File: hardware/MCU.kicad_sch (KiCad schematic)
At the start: 5 parts

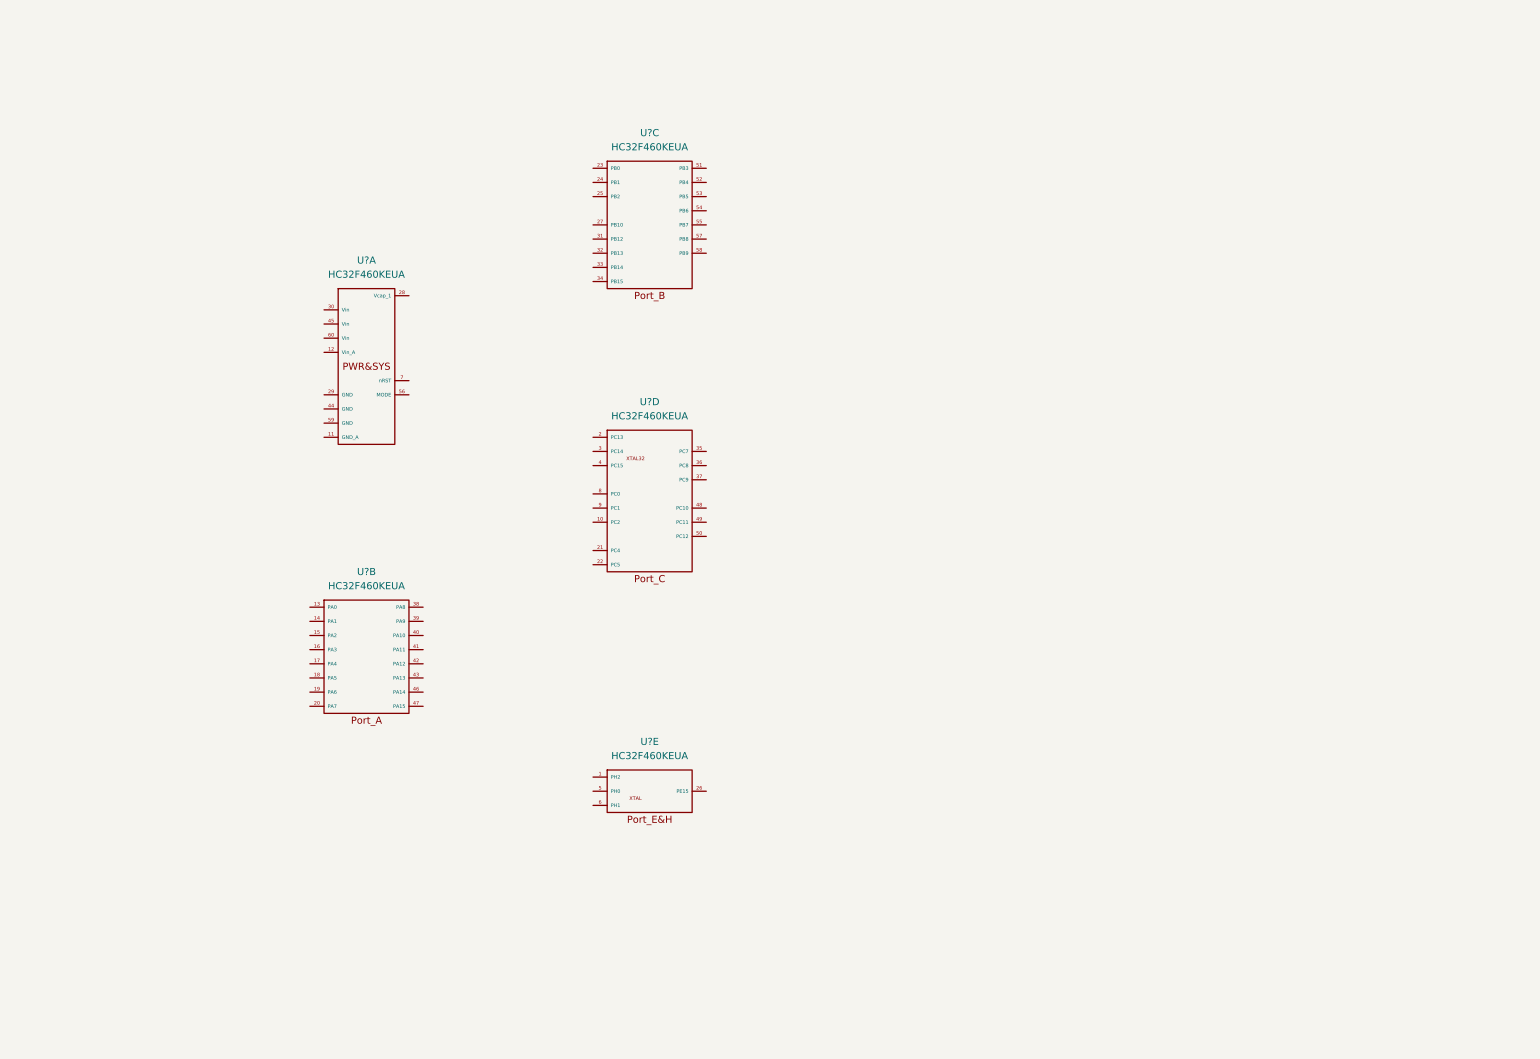
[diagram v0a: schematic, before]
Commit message: Update MCU and Base_PWR.
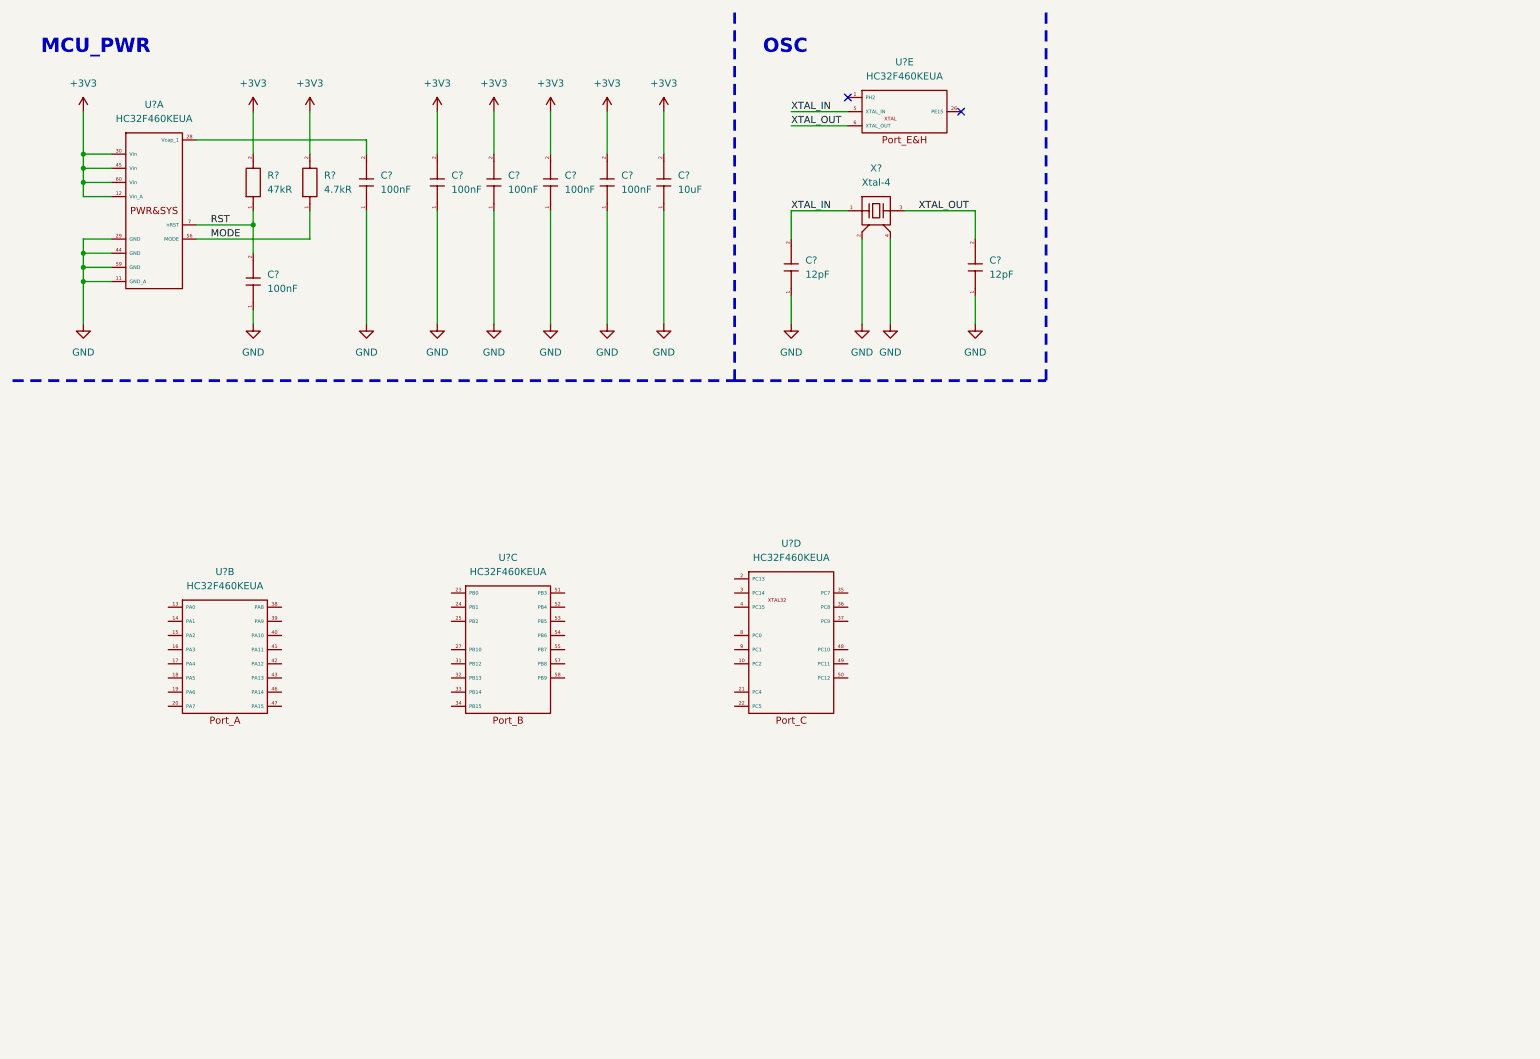
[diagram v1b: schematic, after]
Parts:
- added C? (x6): 100nF, GENERAL_RCL_SMD:C0402(1005M), symbol Basic_passive_components:Capacitor
- added C?: 10uF, GENERAL_RCL_SMD:C0603(1608M), symbol Basic_passive_components:Capacitor
- added C? (x2): 12pF, GENERAL_RCL_SMD:C0402(1005M), symbol Basic_passive_components:Capacitor
- added R?: 4.7kR, GENERAL_RCL_SMD:C0402(1005M), symbol Basic_passive_components:Resistor
- added R?: 47kR, GENERAL_RCL_SMD:C0402(1005M), symbol Basic_passive_components:Resistor
- added X?: Xtal-4, symbol Basic_crystal_and_oscillator:Xtal-4
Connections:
- net XTAL_IN: now reaches U?.5 (PH0)
- net XTAL_IN: now also C?.2, X?.1
- net XTAL_OUT: now reaches U?.6 (PH1)
- net XTAL_OUT: now also C?.2, X?.3
- net GND: now reaches U?.11 (GND_A)
- net GND: now also U?.29 (GND), U?.44 (GND), U?.59 (GND), C?.1, C?.1, C?.1, C?.1, C?.1, C?.1, C?.1, C?.1, C?.1, X?.2, X?.4
- net +3V3: now reaches U?.12 (Vin_A)
- net +3V3: now also U?.30 (Vin), U?.45 (Vin), U?.60 (Vin), C?.2, C?.2, C?.2, C?.2, C?.2, R?.2, R?.2
- net at U?.28 (Vcap_1): now also C?.2
- net MODE: now reaches U?.56 (MODE)
- net MODE: now also R?.1
- net RST: now reaches U?.7 (nRST)
- net RST: now also C?.2, R?.1
- no-connect marks 0 -> 2
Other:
- note added: "MCU_PWR"
- note added: "OSC"
- moved on the sheet: U?A, U?B, U?C, U?D, U?E

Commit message: Daily update
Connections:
- net GND: now also U?.EP
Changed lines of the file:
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@@
   (junction (at 25.4 60.96) (diameter 0) (color 0 0 0 0)
+  )
+  (junction (at 25.4 53.34) (diameter 0) (color 0 0 0 0)
   )
   (junction (at 55.88 50.8) (diameter 0) (color 0 0 0 0)
@@
     (stroke (width 0) (type default) (color 0 0 0 0))
   )
+  (wire (pts (xy 30.48 50.8) (xy 25.4 50.8))
+    (stroke (width 0) (type default) (color 0 0 0 0))
+  )
   (wire (pts (xy 25.4 43.18) (xy 25.4 45.72))
+    (stroke (width 0) (type default) (color 0 0 0 0))
+  )
+  (wire (pts (xy 25.4 50.8) (xy 25.4 53.34))
     (stroke (width 0) (type default) (color 0 0 0 0))
   )
@@
     (pin "4")
   )
-  (symbol (lib_id "Integrated-circuit_micro-controller:HC32F460KEUA") (at 38.1 48.26 0) (unit 1)
+  (symbol (lib_name "HC32F460KEUA_1") (lib_id "Integrated-circuit_micro-controller:HC32F460KEUA") (at 38.1 48.26 0) (unit 1)
     (in_bom yes) (on_board yes) (fields_autoplaced)
     (property "Reference" "U?" (id 0) (at 38.1 29.21 0))
@@
     (pin "60")
     (pin "7")
+    (pin "EP")
     (pin "13")
     (pin "14")

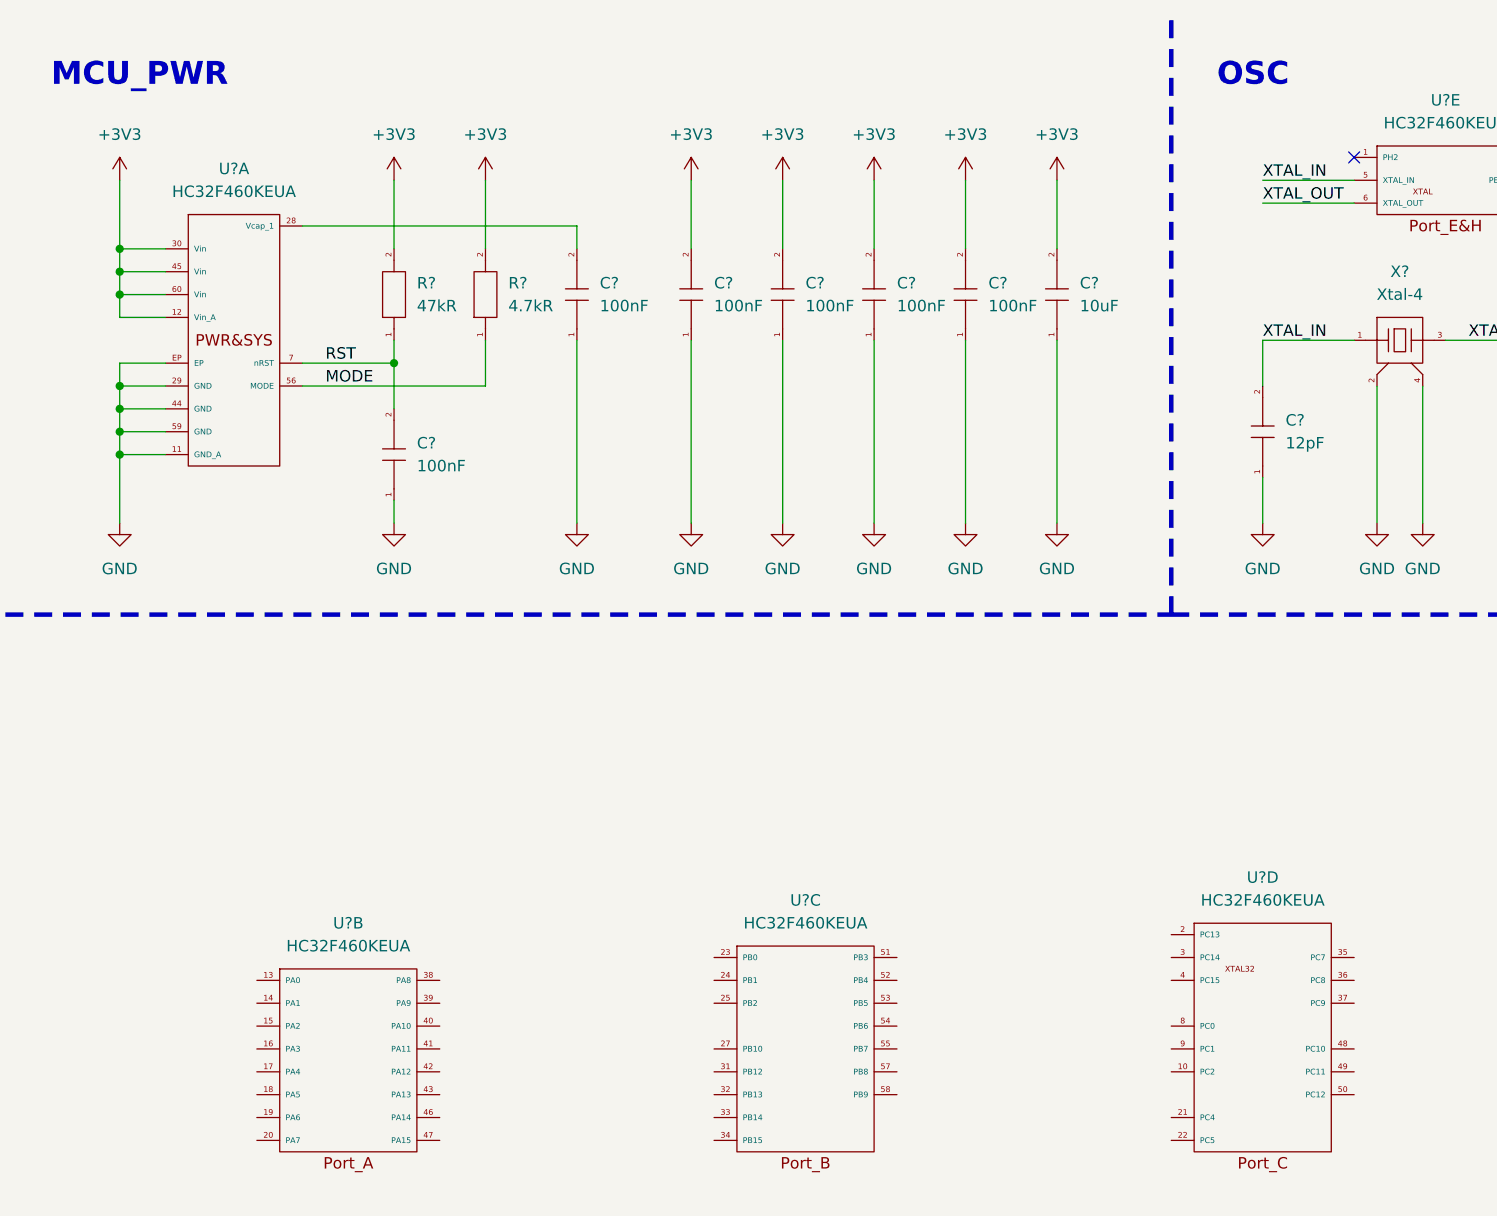
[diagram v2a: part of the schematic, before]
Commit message: Update symbols
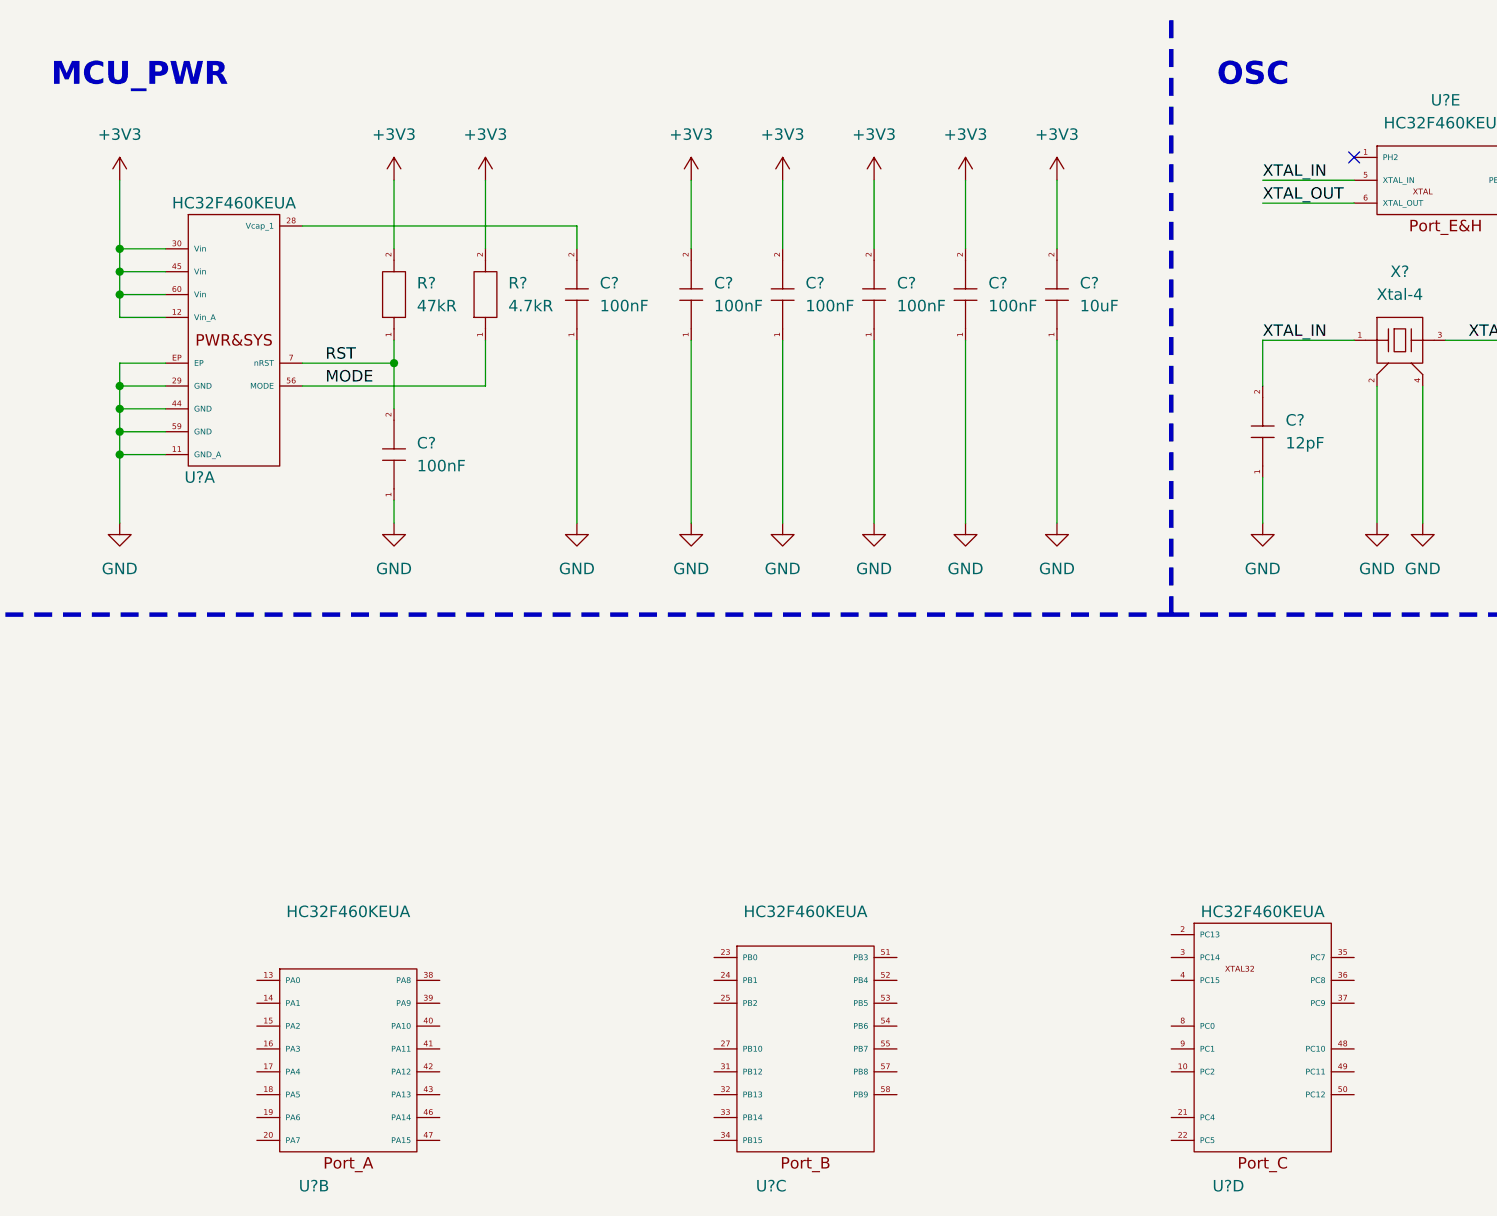
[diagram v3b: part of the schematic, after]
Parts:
- U? (x5): footprint GENERAL_MIDDLE-SEMI_SMD:QFN-7070_60 -> 004_GN_MIDDLE-SEMI_SMD:QFN-60_7070; symbol Integrated-circuit_micro-controller:HC32F460KEUA -> 107_IntegratedCircuit_MicroController:HC32F460KEUA; Symbol type (none) -> Specified Device

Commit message: Nightly update
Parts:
- removed C? (x4): 100nF, GENERAL_RCL_SMD:C0402(1005M), symbol Basic_passive_components:Capacitor
- removed C?: 10uF, GENERAL_RCL_SMD:C0603(1608M), symbol Basic_passive_components:Capacitor
- removed C?: 12pF, GENERAL_RCL_SMD:C0402(1005M), symbol Basic_passive_components:Capacitor
- added C? (x5): 100nF, 001_GN_RCL_SMD:C0402(1005M), symbol 001_Basic_PassiveComponents:101_Capacitor
- added C?: 12pF, 001_GN_RCL_SMD:C0402(1005M), symbol 001_Basic_PassiveComponents:101_Capacitor
- C? (x3): footprint GENERAL_RCL_SMD:C0402(1005M) -> 001_GN_RCL_SMD:C0402(1005M); symbol Basic_passive_components:Capacitor -> 001_Basic_PassiveComponents:101_Capacitor; Symbol type (none) -> Alternate Source
- R? (x2): footprint GENERAL_RCL_SMD:C0402(1005M) -> 001_GN_RCL_SMD:R0402(1005M); symbol Basic_passive_components:Resistor -> 001_Basic_PassiveComponents:001_Resistor; Symbol type (none) -> Alternate Source
- X?: footprint (none) -> 006_GN_XTAL_OSC_SMD:SMD-4_3225; symbol Basic_crystal_and_oscillator:Xtal-4 -> 003_Basic_CrystalAndOscillator:002_Xtal-4; Symbol type (none) -> Alternate Source
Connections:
- net +3V3: now also C?.2, C?.2, C?.2, C?.2, C?.2
- net GND: now also C?.1, C?.1, C?.1, C?.1, C?.1, C?.1
- net XTAL_OUT: now also C?.2

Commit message: Nightly Update
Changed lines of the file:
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@@
   (symbol (lib_id "107_IntegratedCircuit_MicroController:HC32F460KEUA") (at 152.4 127 0) (unit 4)
     (in_bom yes) (on_board yes) (fields_autoplaced)
-    (property "Reference" "U?" (id 0) (at 148.59 142.24 0))
-    (property "Value" "HC32F460KEUA" (id 1) (at 152.4 111.76 0))
+    (property "Reference" "U?" (id 0) (at 152.4 107.95 0))
+    (property "Value" "HC32F460KEUA" (id 1) (at 152.4 110.49 0))
     (property "Footprint" "004_GN_MIDDLE-SEMI_SMD:QFN-60_7070" (id 2) (at 152.4 109.22 0)
       (effects (font (size 1.27 1.27)) hide)
@@
   (symbol (lib_id "107_IntegratedCircuit_MicroController:HC32F460KEUA") (at 101.6 127 0) (unit 3)
     (in_bom yes) (on_board yes) (fields_autoplaced)
-    (property "Reference" "U?" (id 0) (at 97.79 142.24 0))
-    (property "Value" "HC32F460KEUA" (id 1) (at 101.6 111.76 0))
+    (property "Reference" "U?" (id 0) (at 101.6 110.49 0))
+    (property "Value" "HC32F460KEUA" (id 1) (at 101.6 113.03 0))
     (property "Footprint" "004_GN_MIDDLE-SEMI_SMD:QFN-60_7070" (id 2) (at 101.6 109.22 0)
       (effects (font (size 1.27 1.27)) hide)
@@
   (symbol (lib_id "107_IntegratedCircuit_MicroController:HC32F460KEUA") (at 38.1 48.26 0) (unit 1)
     (in_bom yes) (on_board yes) (fields_autoplaced)
-    (property "Reference" "U?" (id 0) (at 34.29 63.5 0))
-    (property "Value" "HC32F460KEUA" (id 1) (at 38.1 33.02 0))
+    (property "Reference" "U?" (id 0) (at 38.1 29.21 0))
+    (property "Value" "HC32F460KEUA" (id 1) (at 38.1 31.75 0))
     (property "Footprint" "004_GN_MIDDLE-SEMI_SMD:QFN-60_7070" (id 2) (at 38.1 30.48 0)
       (effects (font (size 1.27 1.27)) hide)
@@
   (symbol (lib_id "107_IntegratedCircuit_MicroController:HC32F460KEUA") (at 50.8 127 0) (unit 2)
     (in_bom yes) (on_board yes) (fields_autoplaced)
-    (property "Reference" "U?" (id 0) (at 46.99 142.24 0))
-    (property "Value" "HC32F460KEUA" (id 1) (at 50.8 111.76 0))
+    (property "Reference" "U?" (id 0) (at 50.8 113.03 0))
+    (property "Value" "HC32F460KEUA" (id 1) (at 50.8 115.57 0))
     (property "Footprint" "004_GN_MIDDLE-SEMI_SMD:QFN-60_7070" (id 2) (at 50.8 109.22 0)
       (effects (font (size 1.27 1.27)) hide)

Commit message: Update schematics
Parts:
- removed U?: HC32F460KEUA, 004_GN_MIDDLE-SEMI_SMD:QFN-60_7070, symbol 107_IntegratedCircuit_MicroController:HC32F460KEUA
- added J?: 001_Circle-1S, symbol 307_Link_PowerJack:001_Circle-1S
- added J? (x2): Conn_01x02, symbol 302_Link_W2B-Connector:Conn_01x02
- added R? (x2): 150kR, 001_GN_RCL_SMD:R0402(1005M), symbol 001_Basic_PassiveComponents:001_Resistor
- added R? (x2): 10kR, 001_GN_RCL_SMD:R0402(1005M), symbol 001_Basic_PassiveComponents:001_Resistor
- added S?: Switch-SPDT, symbol ACCS:Switch-SPDT
- X?: footprint 006_GN_XTAL_OSC_SMD:SMD-4_3225 -> 006_GN_XTAL_OSC_SMD:CXO-4_3225
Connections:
- net GND: now also J?.2, J?.2, J?.COM, J?.SHELL, R?.2, R?.2
- net PWM1_L: now reaches U?.32 (PB13)
- net PWM2_L: now reaches U?.33 (PB14)
- net DRV2_EN: now reaches U?.34 (PB15)
- net PW_DRV_EN: now reaches U?.51 (PB3)
- net UART_Tx: now reaches U?.54 (PB6)
- net UART_Rx: now reaches U?.55 (PB7)
- net CAN_Tx: now reaches U?.57 (PB8)
- net CAN_Rx: now reaches U?.58 (PB9)
- net CS1_Buff: now reaches U?.13 (PA0)
- net CS2_Buff: now reaches U?.14 (PA1)
- net VDC_sns: now reaches U?.15 (PA2)
- net VDC_sns: now also R?.1, R?.2
- net VBUS_sns: now reaches U?.16 (PA3)
- net VBUS_sns: now also R?.1, R?.2
- net PWM1_H: now reaches U?.38 (PA8)
- net PWM2_H: now reaches U?.39 (PA9)
- net DRV1_EN: now reaches U?.40 (PA10)
- net SWDIO: now reaches U?.43 (PA13)
- net SWCLK: now reaches U?.46 (PA14)
- new net: J?.1, J?.PWR, S?.2 (COM)
- new net VBUS: J?.1, R?.1
- new net VDC: R?.1, S?.1
- no-connect marks 2 -> 4
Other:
- moved on the sheet: C?, U?B, U?C, U?E, X?

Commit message: Complete schematics
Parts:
- added J4: Conn_01x02, 205_CONN_GH_SMD:GH1.25_V_2, symbol 302_Link_W2B-Connector:Conn_01x02
- added J5, J6: Conn_01x04, 205_CONN_GH_SMD:GH1.25_V_4, symbol 302_Link_W2B-Connector:Conn_01x04
- J1: renamed from J?; footprint (none) -> 204_CONN_AMASS_THD:XT30PW-M
- J2: renamed from J?; footprint (none) -> 208_CONN_CIRCLE:DC044B-1_HT
- J3: renamed from J?; footprint (none) -> 204_CONN_AMASS_THD:XT30PW-F
- S1: renamed from S?; footprint (none) -> ACCS:SW-3_8352_THD
- gave numbers to parts that had none: 17
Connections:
- net +3V3: now also J5.1, J6.1
- net CAN_Rx: now also J4.2
- net CAN_Tx: now also J4.1
- net GND: now also J5.4, J6.4
- net SWCLK: now also J6.3
- net SWDIO: now also J6.2
- net UART_Rx: now also J5.3
- net UART_Tx: now also J5.2
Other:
- note added: "CONN"
- note added: "MCU_IO"
- note added: "Vol_SNS"
- moved on the sheet: C8, C9, J1, J2, R3, R4, R5, R6, S1, U1B, U1C, U1E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
